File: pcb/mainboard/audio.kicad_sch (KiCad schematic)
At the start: 0 parts

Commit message: - pcb: working on power supply
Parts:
- added U?: RK809, symbol symbols:RK809
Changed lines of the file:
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@@
     (comment 4 "This source describes Open Hardware and is licensed under the CERN-OHL-S v2. This ")
   )
+  (symbol (lib_id "symbols:RK809") (at 149.86 71.12 0) (unit 4)
+    (in_bom yes) (on_board yes)
+    (property "Reference" "U?" (id 0) (at 149.86 72.39 0))
+    (property "Value" "RK809" (id 1) (at 149.86 74.93 0))
+    (property "Footprint" "" (id 2) (at 149.86 71.12 0)
+      (effects (font (size 1.27 1.27)) hide)
+    )
+    (property "Datasheet" "" (id 3) (at 149.86 71.12 0)
+      (effects (font (size 1.27 1.27)) hide)
+    )
+    (pin "14")
+    (pin "15")
+    (pin "16")
+    (pin "17")
+    (pin "18")
+    (pin "19")
+    (pin "32")
+    (pin "33")
+    (pin "34")
+    (pin "35")
+    (pin "36")
+    (pin "37")
+    (pin "38")
+    (pin "39")
+    (pin "40")
+    (pin "41")
+    (pin "42")
+    (pin "43")
+    (pin "44")
+    (pin "48")
+  )
 )

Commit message: - Upgrade KiCad to latest version - Working on PM circuits - Initial USB Type-C support - Initial support for LCD
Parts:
- added C? (x2): 2.2uF/10V, Capacitor_SMD:C_0402_1005Metric, symbol Device:C
- added C? (x2): 680pF, symbol Device:C
- added C? (x2): 100nF, Capacitor_SMD:C_0402_1005Metric, symbol Device:C
- added C? (x2): 10uF/10V, Capacitor_SMD:C_0603_1608Metric, symbol Device:C
- added C? (x2): 100pF, symbol Device:C
- added C? (x3): 1uF/10V, Capacitor_SMD:C_0402_1005Metric, symbol Device:C
- added C? (x2): 27pF, symbol Device:C
- added FB? (x2): 180R, Inductor_SMD:L_0603_1608Metric, symbol Device:FerriteBead_Small
- added FB?: 120R, Inductor_SMD:L_0603_1608Metric, symbol Device:FerriteBead_Small
- added J?: Conn_01x02, symbol Connector_Generic:Conn_01x02
- added MK?: Microphone, symbol Device:Microphone
- added R?: 100R, Resistor_SMD:R_0402_1005Metric, symbol Device:R
- added R? (x2): 1.1K, Resistor_SMD:R_0402_1005Metric, symbol Device:R
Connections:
- net I2S3_LRCK: now reaches U?.14 (LRCLK)
- net I2S3_SCLK: now reaches U?.15 (BCLK)
- net I2S3_MCLK: now reaches U?.16 (MCLK)
- net I2S3_SDO: now reaches U?.17 (SDI)
- net I2S3_SDI: now reaches U?.18 (SDO/PDMDATA)
- net at U?.32 (SPK_OUTp): now also FB?.1
- net at U?.33 (VCC_SPK_HP): now also C?.2, FB?.2
- net at U?.34 (SPK_OUTn): now also FB?.1
- net at U?.35 (VCC_CPVSS): now also C?.2
- net at U?.36 (CPn): now also C?.2
- net at U?.37 (CPp): now also C?.1
- net at U?.38 (VCC_CPVDD): now also C?.2
- net at U?.42 (MIC1n): now also C?.1, C?.1, C?.2
- net at U?.43 (MIC1p): now also C?.1, C?.1, C?.2
- net at U?.44 (VCC_1P8A): now also C?.2
- net at U?.48 (VCC_1P8D): now also C?.2
- new net: C?.1, R?.1, R?.1
- new net: C?.2, FB?.2, J?.1 (Pin_1)
- new net: C?.1, FB?.2, J?.2 (Pin_2)
- new net: C?.2, C?.2, MK?.2 (+), R?.1
- new net: C?.1, C?.2, MK?.1 (-), R?.2
- new net +5V_SYS: FB?.1
- new net +VCCIO_ACODEC: R?.2
- new net GND: C?.1, C?.1, C?.1, C?.1, C?.1, C?.1, C?.1, C?.2, C?.2, C?.2, R?.2
- no-connect marks 0 -> 1
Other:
- note added: "8ohm/1.3W"
- note added: "Audio Jack TBD"

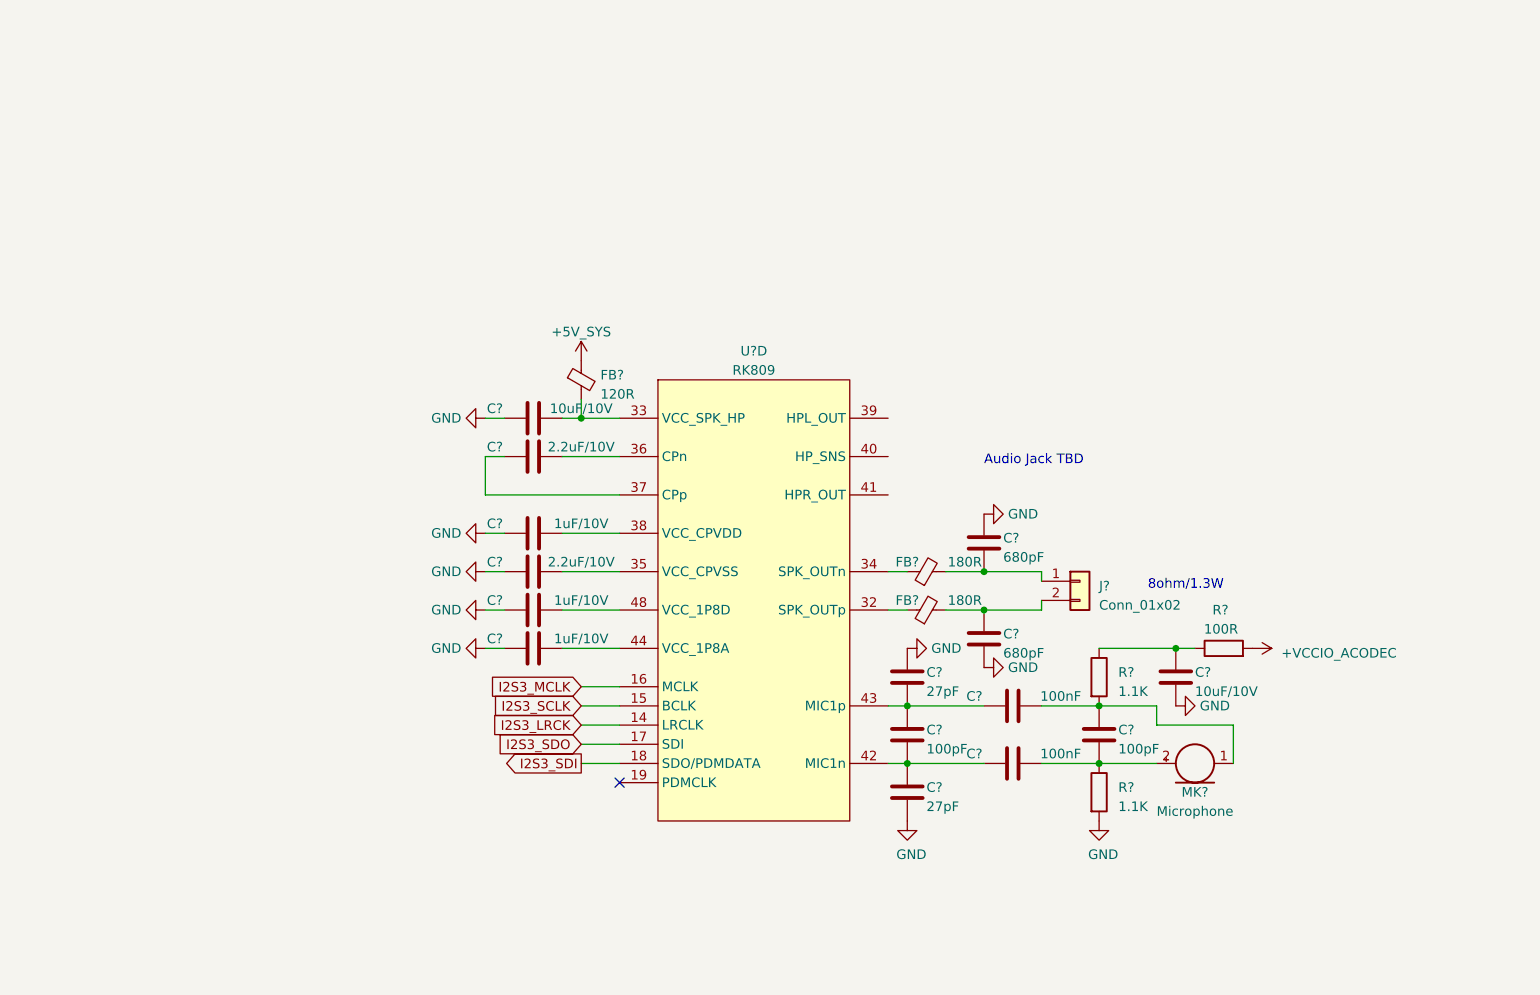
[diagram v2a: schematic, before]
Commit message: - pcb: switch to imx7 for the prototype
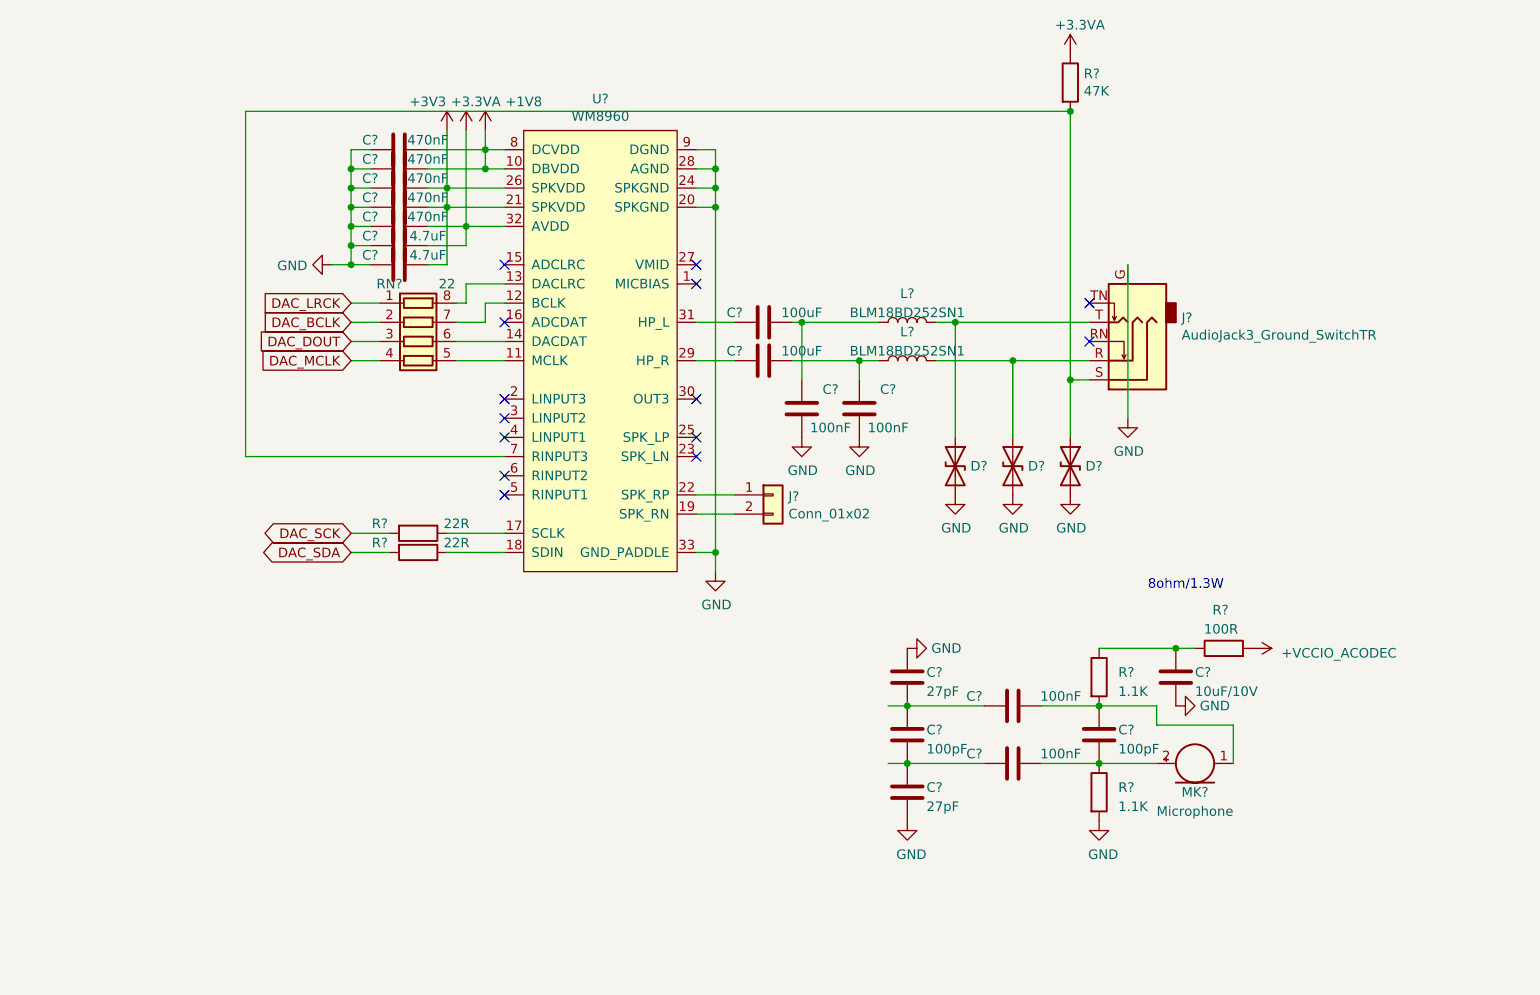
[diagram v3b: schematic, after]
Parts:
- removed C? (x2): 2.2uF/10V, Capacitor_SMD:C_0402_1005Metric, symbol Device:C
- removed C? (x2): 680pF, symbol Device:C
- removed C?: 10uF/10V, Capacitor_SMD:C_0603_1608Metric, symbol Device:C
- removed C? (x3): 1uF/10V, Capacitor_SMD:C_0402_1005Metric, symbol Device:C
- removed FB? (x2): 180R, Inductor_SMD:L_0603_1608Metric, symbol Device:FerriteBead_Small
- removed FB?: 120R, Inductor_SMD:L_0603_1608Metric, symbol Device:FerriteBead_Small
- removed J?: Conn_01x02, symbol Connector_Generic:Conn_01x02
- removed U?: RK809, symbol symbols:RK809
- added C? (x2): 4.7uF, Capacitor_SMD:C_0603_1608Metric, symbol Device:C
- added C? (x2): 100nF, Capacitor_SMD:C_0402_1005Metric, symbol Device:C
- added C? (x5): 470nF, Capacitor_SMD:C_0402_1005Metric, symbol Device:C
- added C? (x2): 100uF, Capacitor_SMD:C_1206_3216Metric, symbol Device:C
- added D? (x3): ESD5B5.0ST1G, Diode_SMD:D_SOD-523, symbol Device:D_TVS
- added J?: Conn_01x02, Connector_PinHeader_2.00mm:PinHeader_1x02_P2.00mm_Vertical, symbol Connector_Generic:Conn_01x02
- added J?: AudioJack3_Ground_SwitchTR, footprint:PJ-327E, symbol Connector:AudioJack3_Ground_SwitchTR
- added L? (x2): BLM18BD252SN1, Inductor_SMD:L_0603_1608Metric, symbol Device:L
- added R?: 47K, Resistor_SMD:R_0402_1005Metric, symbol Device:R
- added R? (x2): 22R, Resistor_SMD:R_0402_1005Metric, symbol Device:R
- added RN?: 22, Resistor_SMD:R_Array_Convex_4x0402, symbol Device:R_Pack04
- added U?: WM8960, Package_DFN_QFN:QFN-32-1EP_5x5mm_P0.5mm_EP3.6x3.6mm, symbol symbols:WM8960
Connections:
- net GND: now also C?.1, C?.1, C?.2, C?.2, C?.2, C?.2, C?.2, C?.2, C?.2, D?.2 (A2), D?.2 (A2), D?.2 (A2), J?.G, U?.20 (SPKGND), U?.24 (SPKGND), U?.28 (AGND), U?.33 (GND_PADDLE), U?.9 (DGND)
- new net: C?.2, C?.2, L?.1 (x2)
- new net: J?.1 (Pin_1), U?.22 (SPK_RP)
- new net: J?.2 (Pin_2), U?.19 (SPK_RN)
- new net: D?.1 (A1), J?.R, L?.2
- new net: RN?.5 (R4.2), U?.11 (MCLK)
- new net: RN?.6 (R3.2), U?.14 (DACDAT)
- new net: RN?.7 (R2.2), U?.12 (BCLK)
- new net: RN?.8 (R1.2), U?.13 (DACLRC)
- new net: D?.1 (A1), J?.T, L?.2
- new net: C?.1, U?.29 (HP_R)
- new net: D?.1 (A1), J?.S, R?.2, U?.7 (RINPUT3)
- new net: R?.1, U?.17 (SCLK)
- new net: R?.1, U?.18 (SDIN)
- new net: C?.1, U?.31 (HP_L)
- new net +1V8: C?.1, C?.1, U?.10 (DBVDD), U?.8 (DCVDD)
- new net +3.3VA: C?.1, C?.1, R?.1, U?.32 (AVDD)
- new net +3V3: C?.1, C?.1, C?.1, U?.21 (SPKVDD), U?.26 (SPKVDD)
- new net DAC_BCLK: RN?.2 (R2.1)
- new net DAC_DOUT: RN?.3 (R3.1)
- new net DAC_LRCK: RN?.1 (R1.1)
- new net DAC_MCLK: RN?.4 (R4.1)
- new net DAC_SCK: R?.2
- new net DAC_SDA: R?.2
- no-connect marks 1 -> 14
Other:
- note removed: "Audio Jack TBD"

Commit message: - pcb: working on r0p1 sch
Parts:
- removed C?: 10uF/10V, Capacitor_SMD:C_0603_1608Metric, symbol Device:C
- removed C? (x2): 100pF, symbol Device:C
- removed C? (x2): 27pF, symbol Device:C
- removed R?: 100R, Resistor_SMD:R_0402_1005Metric, symbol Device:R
- removed R?: 1.1K, Resistor_SMD:R_0402_1005Metric, symbol Device:R
- removed R? (x2): 22R, Resistor_SMD:R_0402_1005Metric, symbol Device:R
- removed RN?: 22, Resistor_SMD:R_Array_Convex_4x0402, symbol Device:R_Pack04
- added C? (x2): 1uF, Capacitor_SMD:C_0402_1005Metric, symbol Device:C
- added C?: 100nF, Capacitor_SMD:C_0402_1005Metric, symbol Device:C
- added J?: Conn_01x02, Connector_PinHeader_2.00mm:PinHeader_1x02_P2.00mm_Vertical, symbol Connector_Generic:Conn_01x02
- added MK?: Microphone, symbol Device:Microphone
- added R? (x5): 22R, Resistor_SMD:R_0402_1005Metric, symbol Device:R
- added R?: 2.2K, Resistor_SMD:R_0402_1005Metric, symbol Device:R
- C? (x2): value 100nF -> 1uF
- R?: value 1.1K -> 2.2K
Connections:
- net +1V8: no longer C?.1, U?.10 (DBVDD)
- net +3V3: now also C?.1, U?.10 (DBVDD)
- net GND: now also C?.2, MK?.2 (+), U?.27 (VMID), C?.2, C?.2, MK?.2 (+)
- net MICBIAS: now reaches R?.1
- net MICBIAS: now also U?.1 (MICBIAS), C?.1, R?.1
- net at C?.1: now also U?.4 (LINPUT1)
- net at C?.1: now also U?.3 (LINPUT2)
- net at U?.11 (MCLK): now also R?.2
- net at U?.14 (DACDAT): now also R?.2
- net at U?.12 (BCLK): now also R?.2
- net at U?.13 (DACLRC): now also U?.15 (ADCLRC), R?.2
- net at U?.16 (ADCDAT): now also R?.2
- net I2C1_SCL: now reaches U?.17 (SCLK)
- net I2C1_SDA: now reaches U?.18 (SDIN)
- net at U?.23 (SPK_LN): now also J?.2 (Pin_2)
- net at U?.25 (SPK_LP): now also J?.1 (Pin_1)
- net at U?.5 (RINPUT1): now also C?.1
- net at U?.6 (RINPUT2): now also C?.1
- new net: C?.2, MK?.1 (-), R?.2
- new net SAI1_MCLK: R?.1
- new net SAI1_RXD: R?.1
- new net SAI1_TXC: R?.1
- new net SAI1_TXD: R?.1
- new net SAI1_TXFS: R?.1
- no-connect marks 14 -> 4
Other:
- note removed: "8ohm/1.3W"
- moved on the sheet: C?, D?, J?, L?, MK?, R?, U?

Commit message: - pcb: r0p1 sch draft
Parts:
- gave numbers to parts that had none: 35

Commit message: - pcb: start r0p1 layout
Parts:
- removed D701, D702, D703: ESD5B5.0ST1G, Diode_SMD:D_SOD-523, symbol Device:D_TVS
- removed J703: AudioJack3_Ground_SwitchTR, footprint:PJ-327E, symbol Connector:AudioJack3_Ground_SwitchTR
- added C717, C718: 100nF, Capacitor_SMD:C_0402_1005Metric, symbol Device:C
- added C719, C720: 470nF, Capacitor_SMD:C_0402_1005Metric, symbol Device:C
- added J703: AudioJack3_SwitchT, footprints:Jack_3.5mm_PJ327E_5A, symbol symbols:AudioJack3_SwitchT
- added L703, L704, L705, L706: 15uH, Inductor_SMD:L_0603_1608Metric, symbol Device:L
- L701, L702: value BLM18BD252SN1 -> 120R
- MK701, MK702: footprint (none) -> Connector_PinSocket_1.27mm:PinSocket_1x02_P1.27mm_Vertical
- R708: value 47K -> 100K
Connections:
- net +3.3VA: no longer C709.1, C710.1, U701.32 (AVDD)
- net +3V3: now also L701.2, L702.2; no longer C706.1, C707.1, C708.1, C711.1, U701.10 (DBVDD), U701.21 (SPKVDD), U701.26 (SPKVDD)
- net GND: now also C717.1, C718.1, J703.S
- net at J702.1 (Pin_1): now also C716.2, C720.1, L705.2; no longer U701.22 (SPK_RP)
- net at J702.2 (Pin_2): now also C714.2, C720.2, L706.2; no longer U701.19 (SPK_RN)
- net at U701.25 (SPK_LP): now also L703.1; no longer J701.1 (Pin_1)
- net at U701.23 (SPK_LN): now also L704.1; no longer J701.2 (Pin_2)
- net at R708.2, U701.7 (RINPUT3): now also J703.TN
- new net: C706.1, C707.1, C708.1, C711.1, L701.1, U701.10 (DBVDD), U701.21 (SPKVDD), U701.26 (SPKVDD)
- new net: C718.2, C719.1, J701.1 (Pin_1), L703.2
- new net: C713.2, J703.R
- new net: C712.2, J703.T
- new net: C717.2, C719.2, J701.2 (Pin_2), L704.2
- new net: C709.1, C710.1, L702.1, U701.32 (AVDD)
- new net: L706.1, U701.19 (SPK_RN)
- new net: L705.1, U701.22 (SPK_RP)
- no-connect marks 4 -> 2
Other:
- company: Copyright EI-2030 2021. -> Copyright EI-2030 2021. / Engineer: Wenting Zhang
- title: Archer -> Archer Mainboard
- moved on the sheet: J701, J702
